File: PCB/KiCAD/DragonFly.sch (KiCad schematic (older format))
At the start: 29 parts, among them Q1 MMBFJ310LT1G, T2 1_4, Y1 8Mhz, Y10 8Mhz, Y2 8Mhz, Y3 8Mhz, Y4 8Mhz, Y5 8Mhz, Y6 8Mhz, Y9 8Mhz

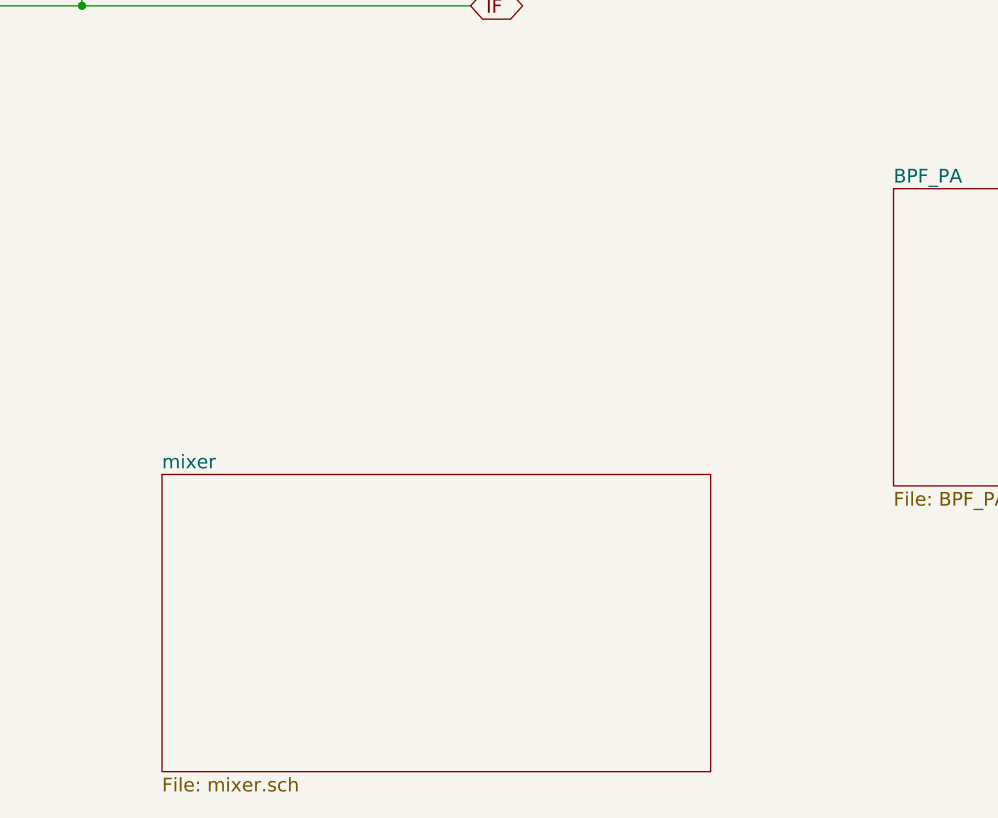
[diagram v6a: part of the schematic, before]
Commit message: denser layout
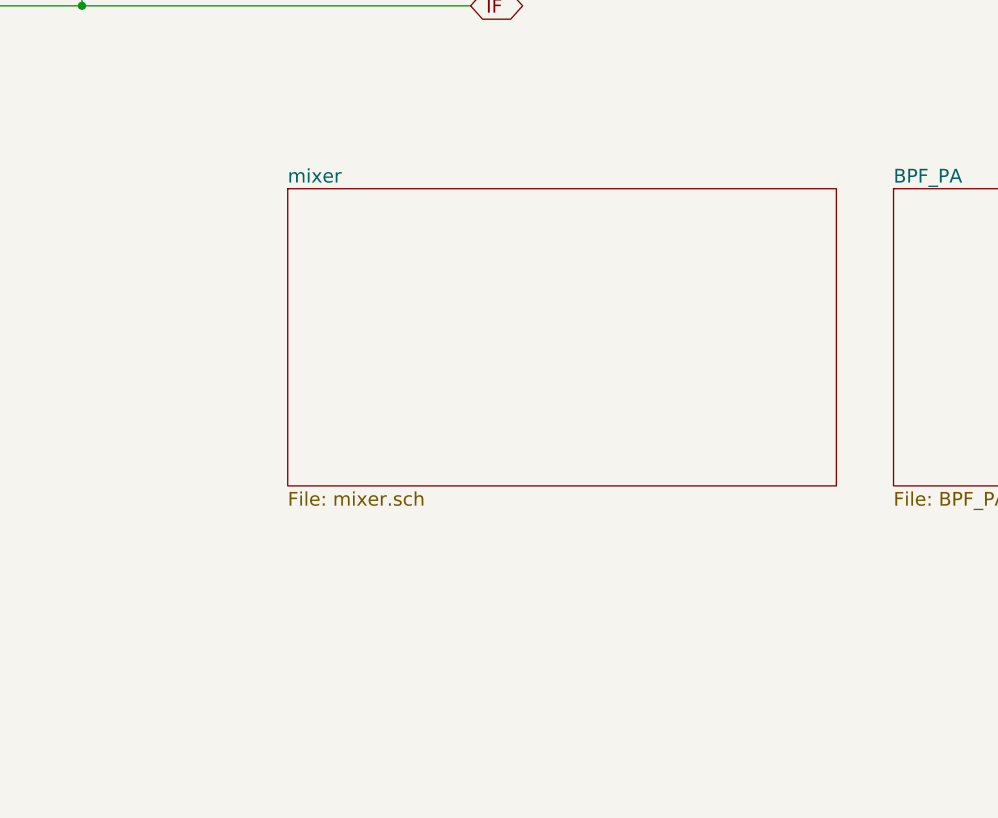
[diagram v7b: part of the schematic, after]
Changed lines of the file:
@@
 $EndComp
 $Sheet
-S 2850 6050 2400 1300
+S 3400 4800 2400 1300
 U 612BEAB5
 F0 "mixer" 60

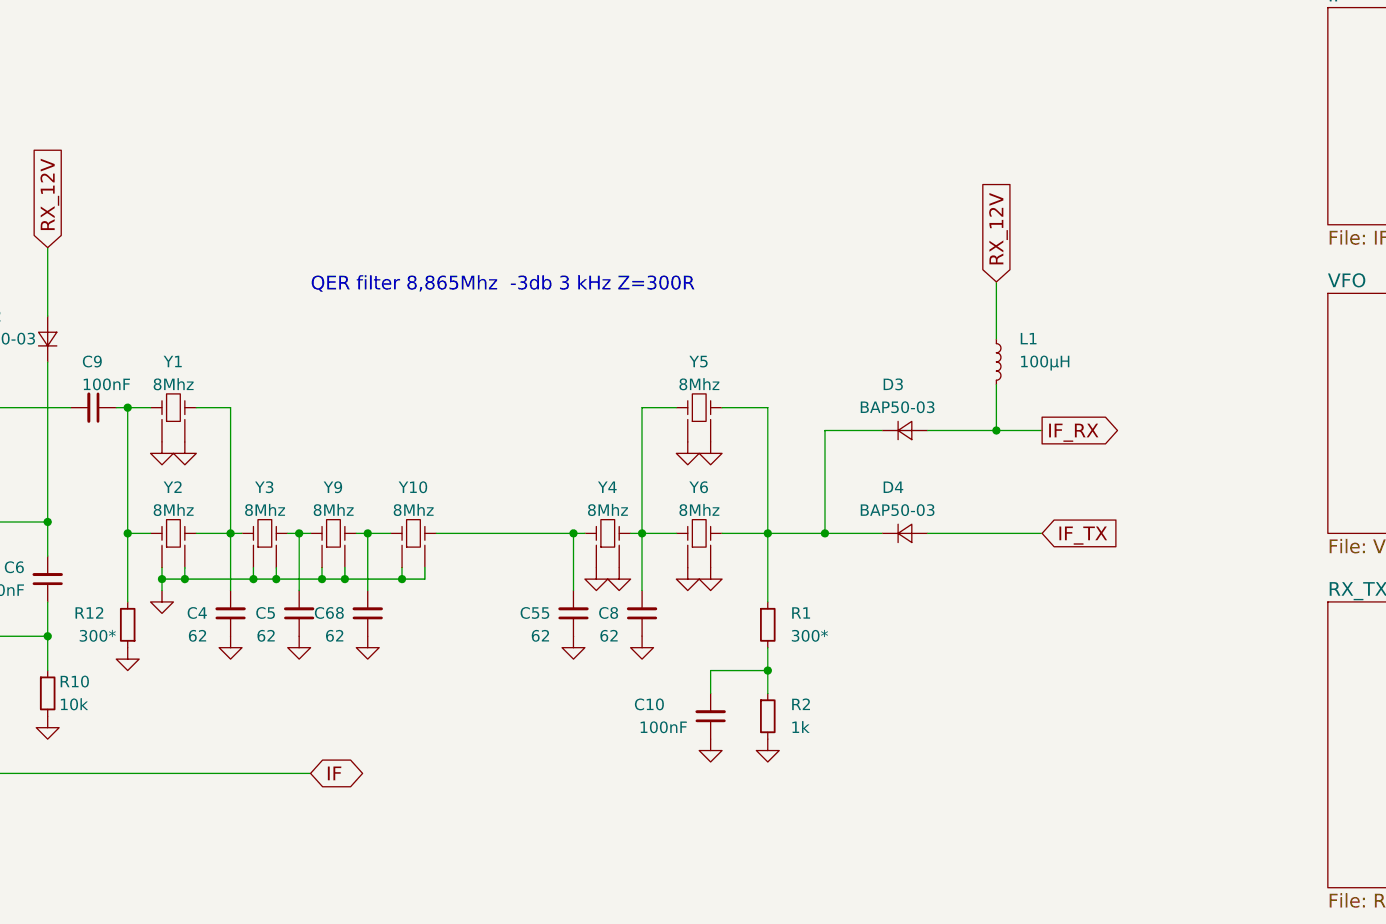
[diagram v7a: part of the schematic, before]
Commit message: add AGC circuit
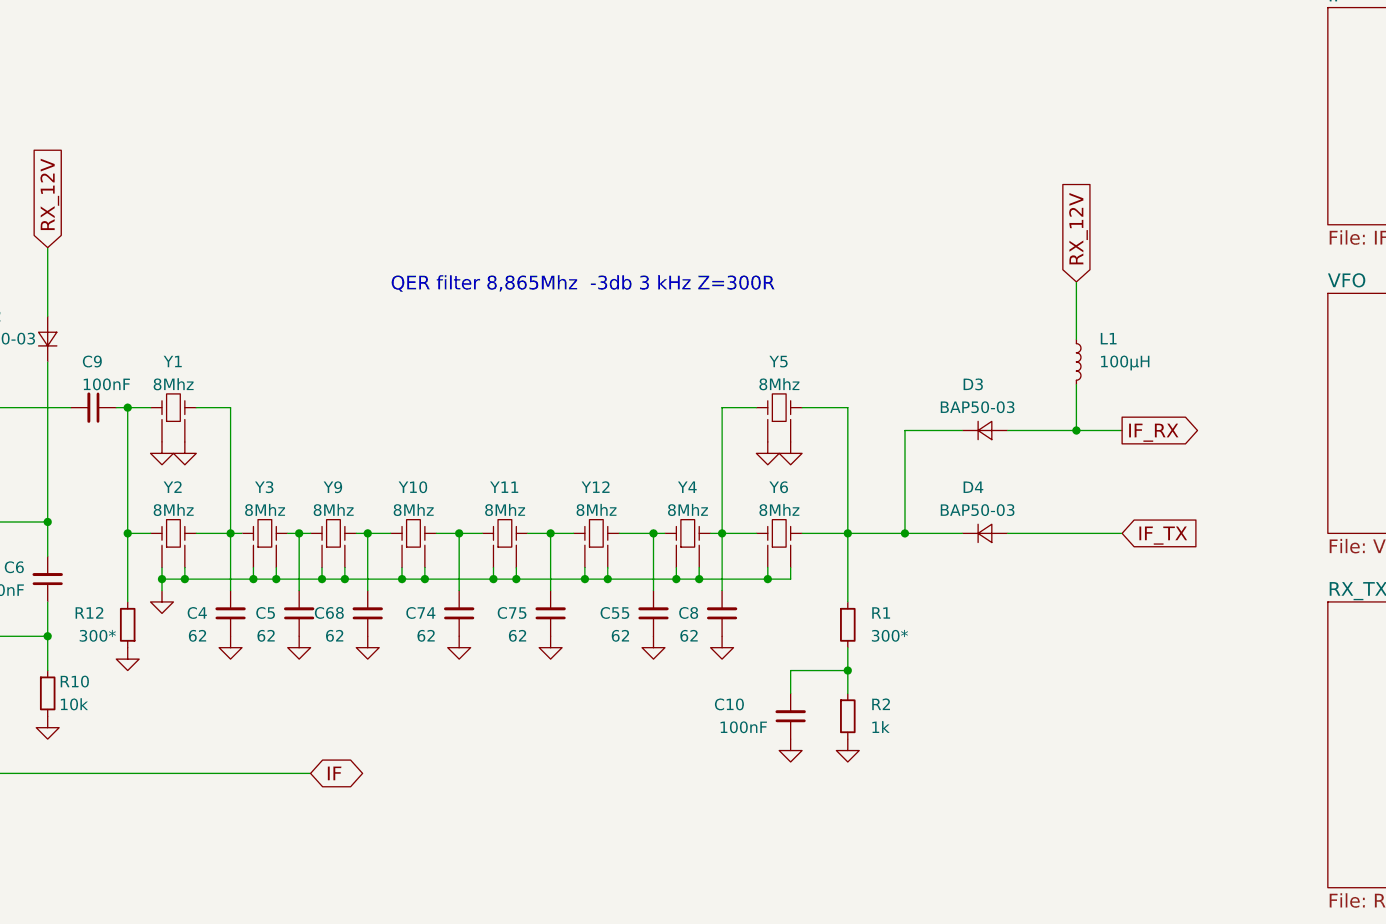
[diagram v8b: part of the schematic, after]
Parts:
- added C74, C75: 62, Capacitors_SMD:C_0805, symbol C_Small
- added Y11, Y12: 8Mhz, DragonFly:Crystal_HC49-U_Vertical, symbol Crystal_Filter
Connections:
- net GND: now also C74.1, C75.1, Y11.3 (GND), Y11.4 (GND), Y12.3 (GND), Y12.4 (GND)
- net at C55.2, Y4.1: now also Y12.2; no longer Y10.2
- new net: C74.2, Y10.2, Y11.1
- new net: C75.2, Y11.2, Y12.1
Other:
- moved on the sheet: C10, C55, C8, D3, D4, L1, R1, R2, Y4, Y5, Y6
